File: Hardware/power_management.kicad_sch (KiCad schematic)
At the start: 32 parts, among them J2 Conn_01x03, SW27 SW_DPDT_x2, U2 BQ24040, U3 BQ51050BRHL, U4 AP22814BW5

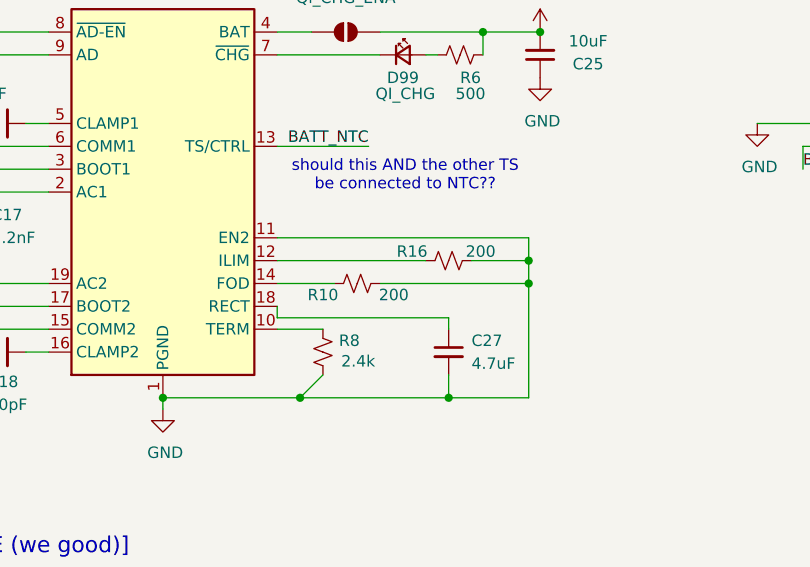
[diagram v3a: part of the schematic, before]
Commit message: Update power management wiring and resistor positions
Added a PWR_FLAG symbol to hornet_kb schematic. Modified power_management schematic wiring, removed and added junctions, and adjusted wire connections for improved power routing. Relocated resistors R10 and R16 to new positions to reflect updated circuit layout.
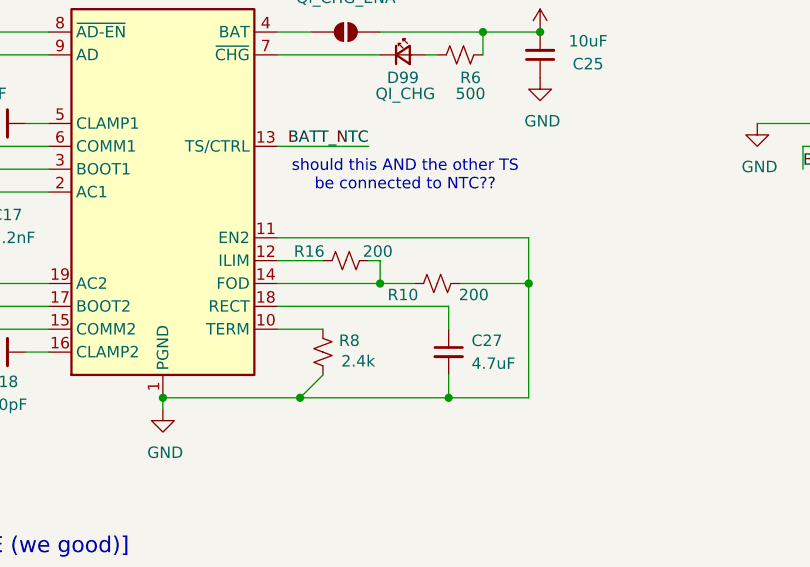
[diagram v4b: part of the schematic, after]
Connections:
- net GND: no longer R16.2
- net at R10.1, U3.14 (FOD): now also R16.2
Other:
- moved on the sheet: R10, R16
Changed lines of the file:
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@@
 	)
 	(junction
-		(at 147.32 143.51)
-		(diameter 0)
-		(color 0 0 0 0)
-	)
-	(junction
 		(at 81.28 76.2)
 		(diameter 0)
@@
 	)
 	(junction
+		(at 130.81 146.05)
+		(diameter 0)
+		(color 0 0 0 0)
+	)
+	(junction
 		(at 21.59 99.06)
 		(diameter 0)
@@
 	(wire
 		(pts
+			(xy 119.38 146.05) (xy 130.81 146.05)
+		)
+		(stroke
+			(width 0)
+			(type default)
+		)
+	)
+	(wire
+		(pts
 			(xy 138.43 158.75) (xy 147.32 158.75)
 		)
@@
 	(wire
 		(pts
-			(xy 147.32 143.51) (xy 147.32 146.05)
+			(xy 147.32 140.97) (xy 147.32 146.05)
 		)
 		(stroke
@@
 	(wire
 		(pts
-			(xy 119.38 149.86) (xy 119.38 148.59)
-		)
-		(stroke
-			(width 0)
-			(type default)
-		)
-	)
-	(wire
-		(pts
-			(xy 147.32 143.51) (xy 140.97 143.51)
-		)
-		(stroke
-			(width 0)
-			(type default)
-		)
-	)
-	(wire
-		(pts
 			(xy 66.04 137.16) (xy 67.31 135.89)
 		)
@@
 	(wire
 		(pts
-			(xy 125.73 146.05) (xy 119.38 146.05)
+			(xy 134.62 146.05) (xy 130.81 146.05)
 		)
 		(stroke
@@
 	(wire
 		(pts
-			(xy 147.32 140.97) (xy 147.32 143.51)
+			(xy 74.93 130.81) (xy 72.39 133.35)
 		)
 		(stroke
@@
 	(wire
 		(pts
-			(xy 74.93 130.81) (xy 72.39 133.35)
+			(xy 38.1 85.09) (xy 38.1 118.11)
 		)
 		(stroke
@@
 	(wire
 		(pts
-			(xy 38.1 85.09) (xy 38.1 118.11)
+			(xy 93.98 146.05) (xy 83.82 146.05)
 		)
 		(stroke
@@
 	(wire
 		(pts
-			(xy 93.98 146.05) (xy 83.82 146.05)
+			(xy 227.33 129.54) (xy 218.44 129.54)
 		)
 		(stroke
@@
 	(wire
 		(pts
-			(xy 227.33 129.54) (xy 218.44 129.54)
+			(xy 83.82 143.51) (xy 83.82 146.05)
 		)
 		(stroke
@@
 	(wire
 		(pts
-			(xy 83.82 143.51) (xy 83.82 146.05)
+			(xy 142.24 118.11) (xy 148.59 118.11)
 		)
 		(stroke
@@
 	(wire
 		(pts
-			(xy 142.24 118.11) (xy 148.59 118.11)
+			(xy 130.81 143.51) (xy 129.54 143.51)
+		)
+		(stroke
+			(width 0)
+			(type default)
+		)
+	)
+	(wire
+		(pts
+			(xy 130.81 143.51) (xy 130.81 146.05)
 		)
 		(stroke
@@
 	(wire
 		(pts
-			(xy 130.81 146.05) (xy 147.32 146.05)
+			(xy 139.7 146.05) (xy 147.32 146.05)
 		)
 		(stroke
@@
 	(wire
 		(pts
-			(xy 138.43 151.13) (xy 138.43 149.86)
+			(xy 138.43 151.13) (xy 138.43 148.59)
 		)
 		(stroke
@@
 	(wire
 		(pts
-			(xy 119.38 143.51) (xy 135.89 143.51)
+			(xy 119.38 143.51) (xy 124.46 143.51)
 		)
 		(stroke
@@
 	(wire
 		(pts
-			(xy 119.38 149.86) (xy 138.43 149.86)
+			(xy 119.38 148.59) (xy 138.43 148.59)
 		)
 		(stroke
@@
 	(symbol
 		(lib_id "Device:R_Small_US")
-		(at 128.27 146.05 90)
+		(at 137.16 146.05 90)
 		(unit 1)
 		(exclude_from_sim no)
@@
 		(dnp no)
 		(property "Reference" "R10"
-			(at 124.46 147.32 90)
+			(at 133.35 147.32 90)
 			(effects
 				(font
@@
 		)
 		(property "Value" "200"
-			(at 132.334 147.32 90)
+			(at 141.224 147.32 90)
 			(effects
 				(font
@@
 		)
 		(property "Footprint" "Resistor_SMD:R_0603_1608Metric"
-			(at 128.27 146.05 0)
+			(at 137.16 146.05 0)
 			(effects
 				(font
@@
 		)
 		(property "Datasheet" "~"
-			(at 128.27 146.05 0)
+			(at 137.16 146.05 0)
 			(effects
 				(font
@@
 		)
 		(property "Description" "Resistor, small US symbol"
-			(at 128.27 146.05 0)
+			(at 137.16 146.05 0)
 			(effects
 				(font
@@
 	(symbol
 		(lib_id "Device:R_Small_US")
-		(at 138.43 143.51 90)
+		(at 127 143.51 90)
 		(unit 1)
 		(exclude_from_sim no)
@@
 		(dnp no)
 		(property "Reference" "R16"
-			(at 134.366 142.494 90)
+			(at 122.936 142.494 90)
 			(effects
 				(font
@@
 		)
 		(property "Value" "200"
-			(at 141.986 142.494 90)
+			(at 130.556 142.494 90)
 			(effects
 				(font
@@
 		)
 		(property "Footprint" "Resistor_SMD:R_0603_1608Metric"
-			(at 138.43 143.51 0)
+			(at 127 143.51 0)
 			(effects
 				(font
@@
 		)
 		(property "Datasheet" "~"
-			(at 138.43 143.51 0)
+			(at 127 143.51 0)
 			(effects
 				(font
@@
 		)
 		(property "Description" "Resistor, small US symbol"
-			(at 138.43 143.51 0)
+			(at 127 143.51 0)
 			(effects
 				(font

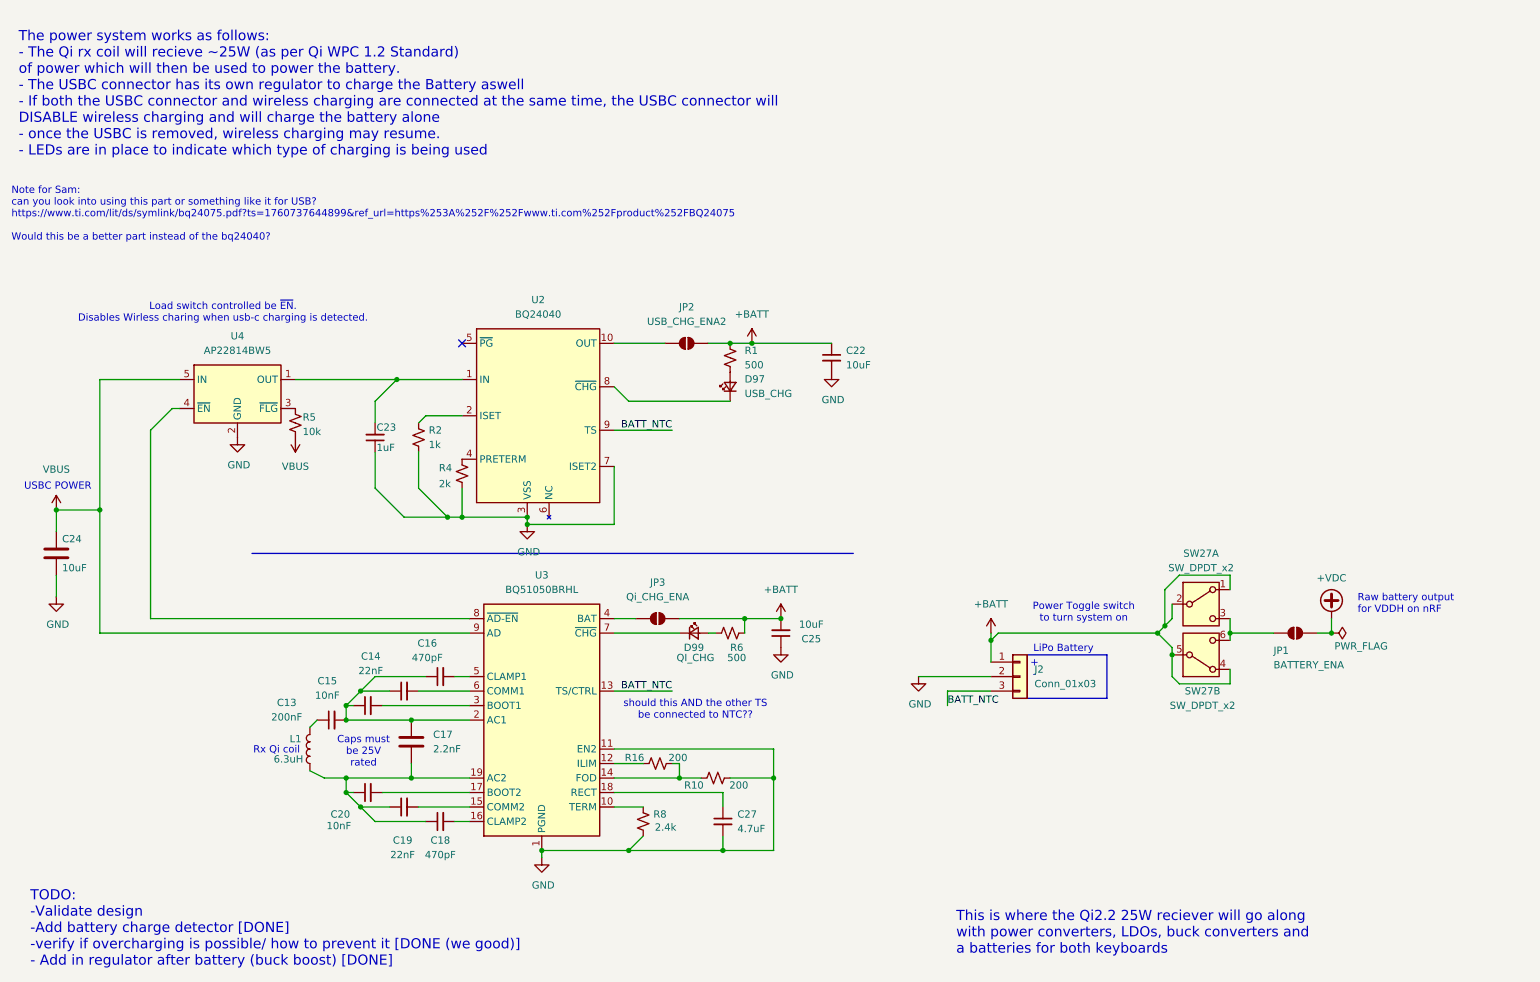
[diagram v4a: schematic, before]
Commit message: Update PCB net names
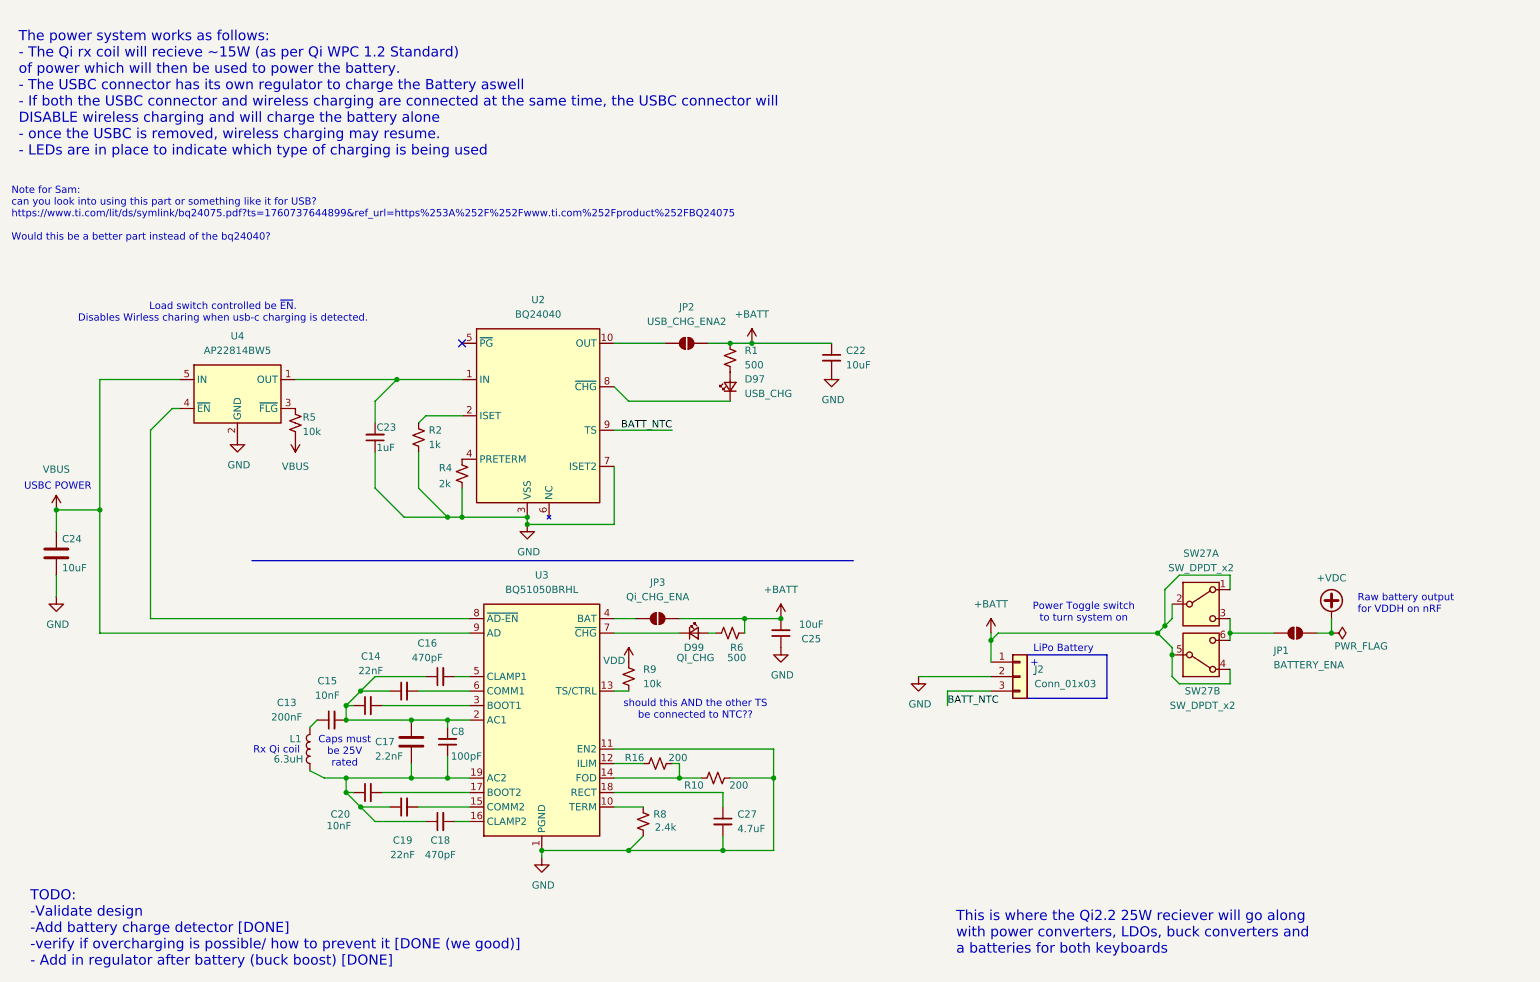
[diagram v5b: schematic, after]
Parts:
- added C8: 100pF, Capacitor_SMD:C_0603_1608Metric, symbol Device:C_Small
- added R9: 10k, symbol Device:R_Small_US
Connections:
- net BATT_NTC: no longer U3.13 (TS/CTRL)
- net at C13.2, C14.1, C15.1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: now also C8.2
- net at C17.2, C18.1, C19.1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: now also C8.1
- new net: R9.2, U3.13 (TS/CTRL)
- new net VDD: R9.1
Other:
- note added: "The power system works as follows: - The Qi rx coil will recieve ~15W (as per Qi WPC 1.2 Standard) of power which will then be used to power the battery. - The USBC connector has its own regulator to charge the Battery aswell - If both the USBC connector and wireless charging are connected at the same time, the USBC connector will DISABLE wireless charging and will charge the battery alone - once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"
- note removed: "The power system works as follows: - The Qi rx coil will recieve ~25W (as per Qi WPC 1.2 Standard) of power which will then be used to power the battery. - The USBC connector has its own regulator to charge the Battery aswell - If both the USBC connector and wireless charging are connected at the same time, the USBC connector will DISABLE wireless charging and will charge the battery alone - once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"

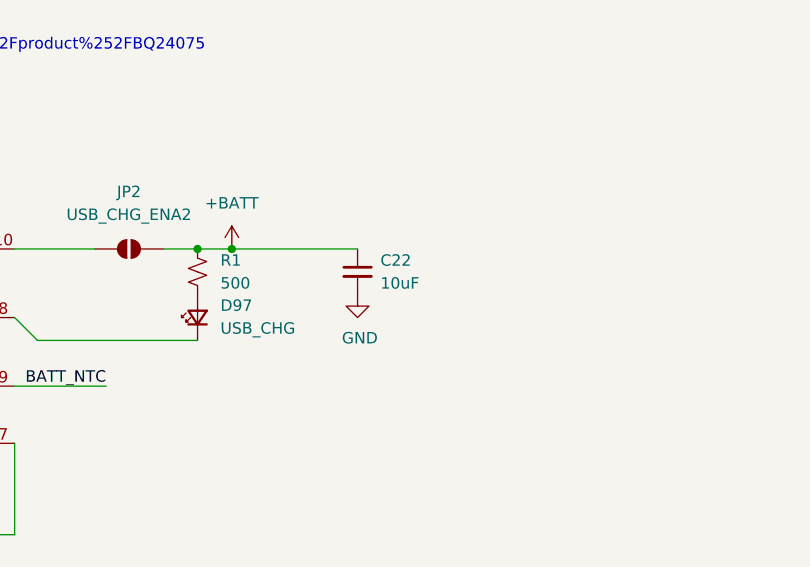
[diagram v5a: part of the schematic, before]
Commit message: Changed C22 cap value
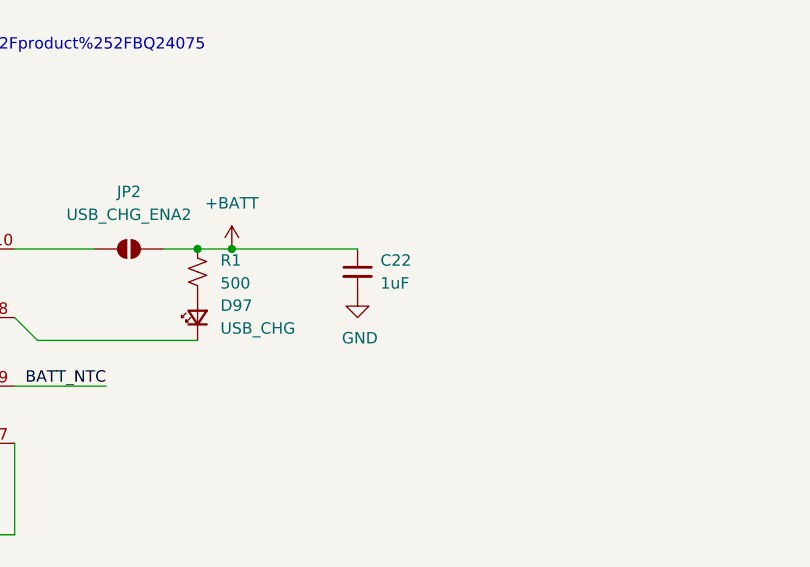
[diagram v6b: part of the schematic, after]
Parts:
- C22: value 10uF -> 1uF
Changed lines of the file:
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@@
 			)
 		)
-		(property "Value" "10uF"
+		(property "Value" "1uF"
 			(at 160.02 73.6662 0)
 			(effects

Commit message: assign footprints (rough draft)
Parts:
- D99: footprint (none) -> LED_SMD:LED_0402_1005Metric
- R9: footprint (none) -> Resistor_SMD:R_0603_1608Metric
- SW27: footprint (none) -> Button_Switch_THT:SW_CK_JS202011CQN_DPDT_Straight
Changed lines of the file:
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@@
 			)
 		)
-		(property "Footprint" ""
+		(property "Footprint" "LED_SMD:LED_0402_1005Metric"
 			(at 133.35 120.65 90)
 			(effects
@@
 			)
 		)
-		(property "Footprint" ""
+		(property "Footprint" "Button_Switch_THT:SW_CK_JS202011CQN_DPDT_Straight"
 			(at 222.25 124.46 0)
 			(effects
@@
 			)
 		)
-		(property "Footprint" ""
+		(property "Footprint" "Resistor_SMD:R_0603_1608Metric"
 			(at 121.92 128.27 0)
 			(effects
@@
 			)
 		)
-		(property "Footprint" ""
+		(property "Footprint" "Button_Switch_THT:SW_CK_JS202011CQN_DPDT_Straight"
 			(at 222.25 115.57 0)
 			(effects

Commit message: delete stale comments and fix erc
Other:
- note removed: "should this AND the other TS be connected to NTC??"
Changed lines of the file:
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@@
 		(rev "1")
 	)
-	(text "should this AND the other TS\nbe connected to NTC??"
-		(exclude_from_sim no)
-		(at 133.604 134.112 0)
-		(effects
-			(font
-				(size 1.27 1.27)
-			)
-		)
-	)
 	(text "Rx Qi coil\n"
 		(exclude_from_sim no)
@@
 	)
 	(junction
+		(at 185.42 125.73)
+		(diameter 0)
+		(color 0 0 0 0)
+	)
+	(junction
 		(at 74.93 151.13)
 		(diameter 0)
@@
 	)
 	(junction
+		(at 168.91 128.27)
+		(diameter 0)
+		(color 0 0 0 0)
+	)
+	(junction
 		(at 83.82 135.89)
 		(diameter 0)
@@
 	(wire
 		(pts
-			(xy 172.72 128.27) (xy 185.42 128.27)
+			(xy 168.91 128.27) (xy 185.42 128.27)
 		)
 		(stroke
@@
 	)
 	(symbol
+		(lib_id "power:PWR_FLAG")
+		(at 185.42 125.73 90)
+		(unit 1)
+		(exclude_from_sim no)
+		(in_bom yes)
+		(on_board yes)
+		(dnp no)
+		(fields_autoplaced yes)
+		(property "Reference" "#FLG05"
+			(at 183.515 125.73 0)
+			(effects
+				(font
+					(size 1.27 1.27)
+				)
+				(hide yes)
+			)
+		)
+		(property "Value" "PWR_FLAG"
+			(at 181.61 125.7299 90)
+			(effects
+				(font
+					(size 1.27 1.27)
+				)
+				(justify left)
+			)
+		)
+		(property "Footprint" ""
+			(at 185.42 125.73 0)
+			(effects
+				(font
+					(size 1.27 1.27)
+				)
+				(hide yes)
+			)
+		)
+		(property "Datasheet" "~"
+			(at 185.42 125.73 0)
+			(effects
+				(font
+					(size 1.27 1.27)
+				)
+				(hide yes)
+			)
+		)
+		(property "Description" "Special symbol for telling ERC where power comes from"
+			(at 185.42 125.73 0)
+			(effects
+				(font
+					(size 1.27 1.27)
+				)
+				(hide yes)
+			)
+		)
+		(pin "1"
+		)
+		(instances
+			(project ""
+				(path "/c35084ab-104c-4a4c-9388-a839989b8e3d/20e65fb9-037d-41f9-856c-d800ba40b4b1"
+					(reference "#FLG05")
+					(unit 1)
+				)
+			)
+		)
+	)
+	(symbol
 		(lib_id "power:GND")
 		(at 106.68 160.02 0)
@@
 	)
 	(symbol
+		(lib_id "power:PWR_FLAG")
+		(at 168.91 128.27 90)
+		(unit 1)
+		(exclude_from_sim no)
+		(in_bom yes)
+		(on_board yes)
+		(dnp no)
+		(fields_autoplaced yes)
+		(property "Reference" "#FLG07"
+			(at 167.005 128.27 0)
+			(effects
+				(font
+					(size 1.27 1.27)
+				)
+				(hide yes)
+			)
+		)
+		(property "Value" "PWR_FLAG"
+			(at 165.1 128.2699 90)
+			(effects
+				(font
+					(size 1.27 1.27)
+				)
+				(justify left)
+			)
+		)
+		(property "Footprint" ""
+			(at 168.91 128.27 0)
+			(effects
+				(font
+					(size 1.27 1.27)
+				)
+				(hide yes)
+			)
+		)
+		(property "Datasheet" "~"
+			(at 168.91 128.27 0)
+			(effects
+				(font
+					(size 1.27 1.27)
+				)
+				(hide yes)
+			)
+		)
+		(property "Description" "Special symbol for telling ERC where power comes from"
+			(at 168.91 128.27 0)
+			(effects
+				(font
+					(size 1.27 1.27)
+				)
+				(hide yes)
+			)
+		)
+		(pin "1"
+		)
+		(instances
+			(project "hornet_kb"
+				(path "/c35084ab-104c-4a4c-9388-a839989b8e3d/20e65fb9-037d-41f9-856c-d800ba40b4b1"
+					(reference "#FLG07")
+					(unit 1)
+				)
+			)
+		)
+	)
+	(symbol
 		(lib_id "Device:C_Small")
 		(at 90.17 139.7 180)
@@
 	(symbol
 		(lib_id "power:GND")
-		(at 172.72 128.27 0)
+		(at 168.91 128.27 0)
 		(mirror y)
 		(unit 1)
@@
 		(dnp no)
 		(property "Reference" "#PWR013"
-			(at 172.72 134.62 0)
+			(at 168.91 134.62 0)
 			(effects
 				(font
@@
 		)
 		(property "Value" "GND"
-			(at 172.974 133.096 0)
+			(at 169.164 133.096 0)
 			(effects
 				(font
@@
 		)
 		(property "Footprint" ""
-			(at 172.72 128.27 0)
+			(at 168.91 128.27 0)
 			(effects
 				(font
@@
 		)
 		(property "Datasheet" ""
-			(at 172.72 128.27 0)
+			(at 168.91 128.27 0)
 			(effects
 				(font
@@
 		)
 		(property "Description" "Power symbol creates a global label with name \"GND\" , ground"
-			(at 172.72 128.27 0)
+			(at 168.91 128.27 0)
 			(effects
 				(font
